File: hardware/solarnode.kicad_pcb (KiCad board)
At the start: 2 copper layers, 36 x 42.2 mm, 35 parts, among them IC1 STM32F0xxFxPx, P1 USB_OTG, P2 SWD, P3 C_PANEL, P4 C_BATT, U2 CN3083, U3 MCP1700, U4 RFM69HW, U5 DS18B20, U6 DS18B20

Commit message: Fix open-drain pull-ups to be actual pull-ups
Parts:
- P2: value SWD -> TC2030-CTX
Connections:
- R1 pad 1: GND -> VCC
- R2 pad 2: GND -> VCC
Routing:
- net VCC: track 76.8 -> 82.0 mm
- net GND: track 95.6 -> 92.0 mm, vias 13 -> 12
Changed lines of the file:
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@@
   (general
     (links 91)
-    (no_connects 0)
-    (area 159.245 94.875 205.390101 135.975)
+    (no_connects 1)
+    (area 161.674999 95.924999 197.825001 138.325001)
     (thickness 1.6)
     (drawings 9)
@@
     (mod_text_size 0.4 0.4)
     (mod_text_width 0.1)
-    (pad_size 3.3 3.3)
-    (pad_drill 3.3)
+    (pad_size 0.6 0.6)
+    (pad_drill 0.4)
     (pad_to_mask_clearance 0.2)
     (aux_axis_origin 161.75 138.25)
@@
       (effects (font (size 0.4 0.4) (thickness 0.1)))
     )
-    (fp_text value SWD (at 1.54 -2.516 90) (layer F.SilkS)
+    (fp_text value TC2030-CTX (at 1.54 -2.516 90) (layer F.SilkS)
       (effects (font (size 0.4 0.4) (thickness 0.1)))
     )
@@
     (fp_line (start -0.6 -0.875) (end 0.6 -0.875) (layer F.SilkS) (width 0.15))
     (pad 1 smd rect (at -0.95 0) (size 0.7 1.3) (layers F.Cu F.Paste F.Mask)
-      (net 2 GND))
+      (net 3 VCC))
     (pad 2 smd rect (at 0.95 0) (size 0.7 1.3) (layers F.Cu F.Paste F.Mask)
       (net 8 BATT_CHARGE))
@@
       (net 9 BATT_OK))
     (pad 2 smd rect (at 0.95 0 180) (size 0.7 1.3) (layers F.Cu F.Paste F.Mask)
-      (net 2 GND))
+      (net 3 VCC))
     (model Resistors_SMD.3dshapes/R_0805.wrl
       (at (xyz 0 0 0))
@@
   (segment (start 187 114) (end 183.815 114) (width 0.25) (layer F.Cu) (net 2))
   (segment (start 183.815 114) (end 183.7 114.115) (width 0.25) (layer F.Cu) (net 2))
-  (segment (start 173.55 115.25) (end 173.55 116.5) (width 0.25) (layer F.Cu) (net 2))
-  (segment (start 173.55 114) (end 173.55 115.25) (width 0.25) (layer F.Cu) (net 2))
-  (segment (start 173.55 115.25) (end 172.5 115.25) (width 0.25) (layer F.Cu) (net 2))
-  (via (at 172.5 115.25) (size 0.6) (drill 0.4) (layers F.Cu B.Cu) (net 2))
   (segment (start 181.75 109.5) (end 183 109.5) (width 0.5) (layer F.Cu) (net 2))
   (segment (start 183 109.5) (end 184.5 108) (width 0.5) (layer F.Cu) (net 2))
@@
   (segment (start 164.5 109.7) (end 164.5 111.2125) (width 0.25) (layer F.Cu) (net 2))
   (segment (start 164.5 111.2125) (end 164.25 111.4625) (width 0.25) (layer F.Cu) (net 2))
+  (segment (start 173 111.5) (end 173 113.45) (width 0.25) (layer F.Cu) (net 3))
+  (segment (start 173 113.45) (end 173.55 114) (width 0.25) (layer F.Cu) (net 3))
+  (segment (start 173.55 115.25) (end 173.55 116.5) (width 0.25) (layer F.Cu) (net 3))
+  (segment (start 173.55 114) (end 173.55 115.25) (width 0.25) (layer F.Cu) (net 3))
   (segment (start 180 123) (end 182 123) (width 0.25) (layer F.Cu) (net 3))
   (segment (start 180.552139 124.447861) (end 182 123) (width 0.25) (layer F.Cu) (net 3))

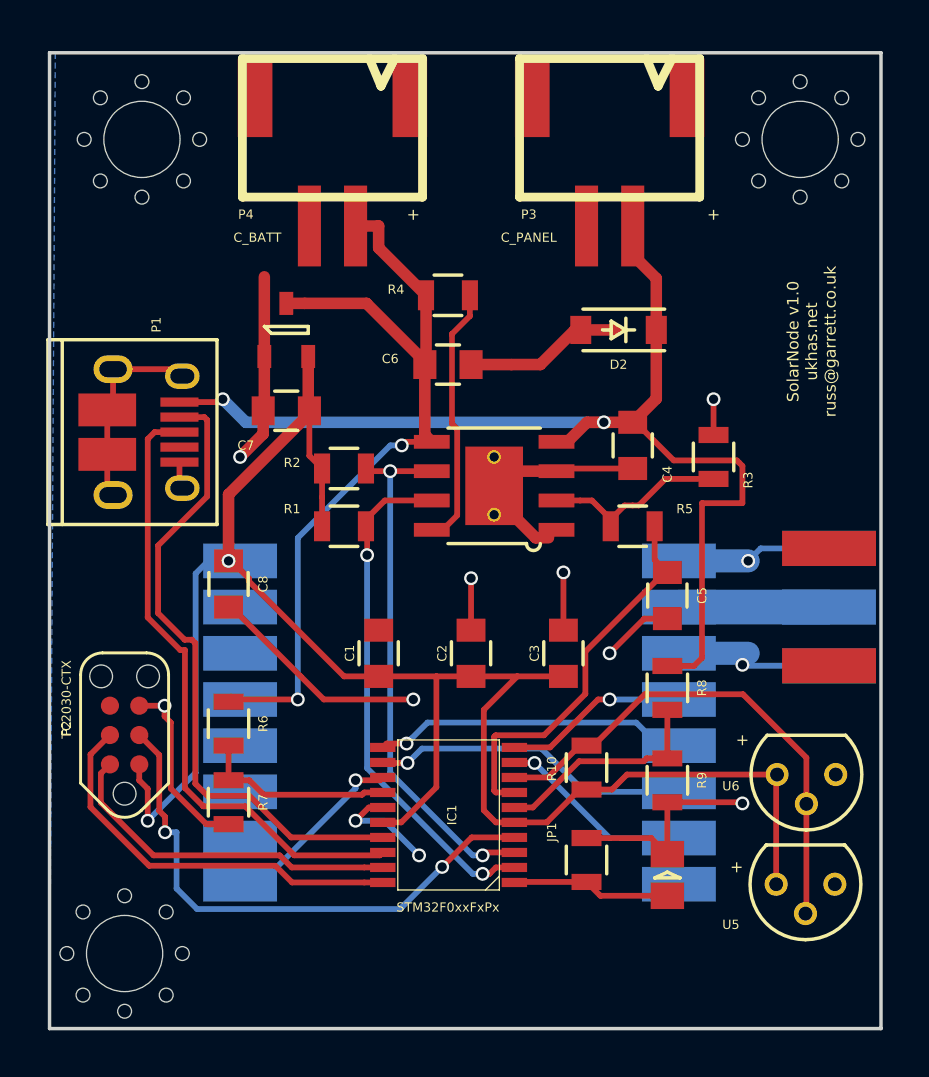
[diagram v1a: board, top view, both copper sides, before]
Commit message: Version 1.1
- Fix incorrect RFM69 SPI wiring
- Remove unneeded pullup resistors on CN3083 open-drain outputs
- Fix silk text sizing so it's actually readable
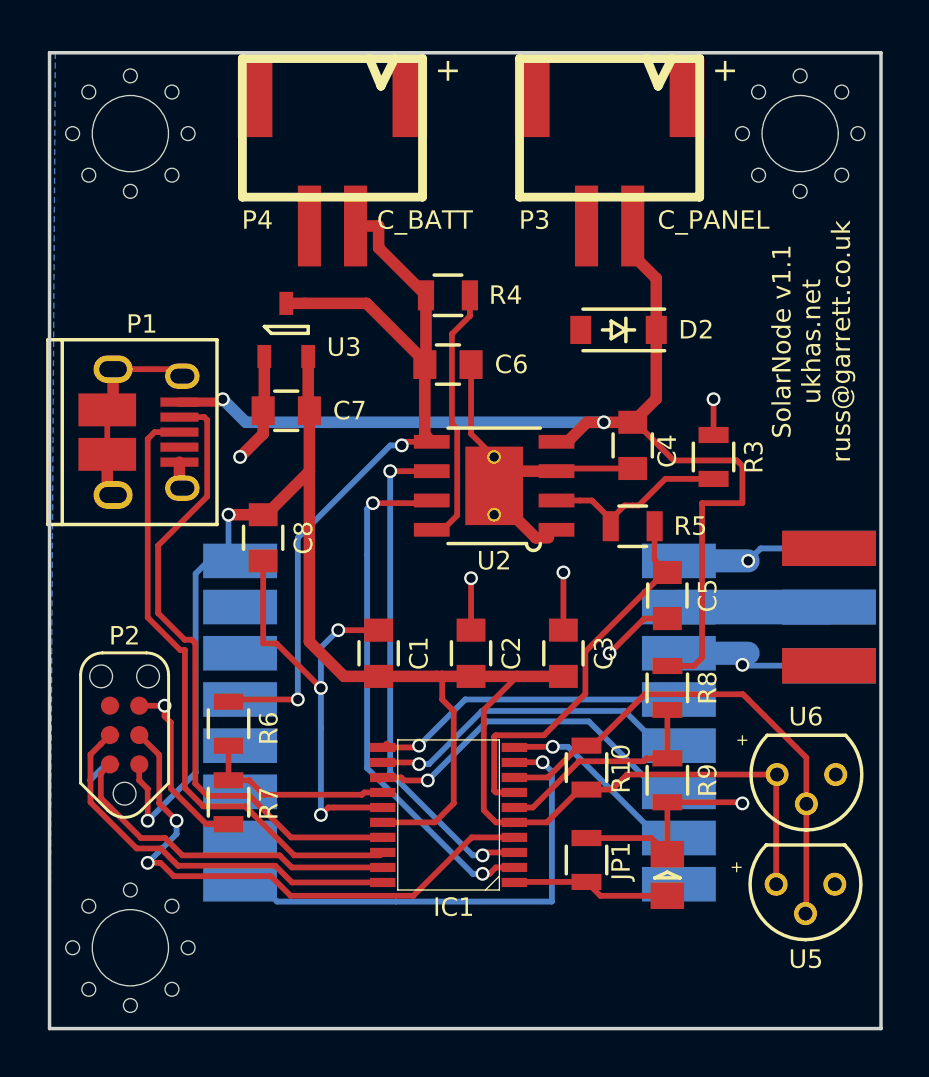
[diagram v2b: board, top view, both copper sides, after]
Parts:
- removed R1, R2: 10k, Resistors_SMD:R_0805
- removed the REF** at (194.2, 99.8)
- removed the REF** at (165.8, 99.8)
- removed the REF** at (165.0, 135.0)
- added REF**: M3_MOUNT, agg:M3_MOUNT, F.Cu at (194.2, 99.5)
- added REF**: M3_MOUNT, agg:M3_MOUNT, F.Cu at (165.2, 134.8)
- added REF**: M3_MOUNT, agg:M3_MOUNT, F.Cu at (165.2, 99.5)
- moved C8 2.50 mm to (171.0, 117.0)
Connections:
- IC1 pad 9: Net-(IC1-Pad9) -> RFM_RST
- P1 pad 4: Net-(P1-Pad4) -> (no net)
- P2 pad 6: Net-(P2-Pad6) -> (no net)
- U4 pad 1: Net-(U4-Pad1) -> (no net)
- U4 pad 10: Net-(U4-Pad10) -> (no net)
- U4 pad 11: Net-(U4-Pad11) -> (no net)
- U4 pad 12: Net-(U4-Pad12) -> (no net)
- U4 pad 13: Net-(U4-Pad13) -> (no net)
- U4 pad 14: Net-(U4-Pad14) -> (no net)
- U4 pad 15: Net-(U4-Pad15) -> (no net)
- U4 pad 2: Net-(IC1-Pad9) -> Net-(IC1-Pad10)
- U4 pad 3: Net-(IC1-Pad12) -> Net-(IC1-Pad13)
- U4 pad 4: Net-(IC1-Pad11) -> Net-(IC1-Pad12)
- U4 pad 5: Net-(IC1-Pad10) -> Net-(IC1-Pad11)
- U4 pad 9: Net-(IC1-Pad13) -> RFM_RST
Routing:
- net RFM_RST: track 0.00 -> 21.3 mm, vias 0 -> 1
- net Net-(IC1-Pad9): track 11.0 -> 0.00 mm, vias 1 -> 0
- net Net-(IC1-Pad13): track 8.30 -> 15.4 mm
- net BATT_OK: track 22.9 -> 21.8 mm
- net (no net): track 0.00 -> 1.06 mm
- net GND: track 92.0 -> 91.2 mm
- net Net-(IC1-Pad10): track 7.98 -> 8.77 mm
- net Net-(IC1-Pad12): track 13.9 -> 14.5 mm
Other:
- board text added: "SolarNode v1.1 ukhas.net russ@garrett.co.uk"
- board text removed: "SolarNode v1.0 ukhas.net russ@garrett.co.uk"

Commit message: Version 1.1 hardware + stencil
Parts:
- removed JP1: Boot, Resistors_SMD:R_0805
- IC1: value STM32F0xxFxPx -> STM32F042F6P6
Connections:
- P1 pad 4: (no net) -> Net-(P1-Pad4)
- P2 pad 6: (no net) -> Net-(P2-Pad6)
- U4 pad 1: (no net) -> Net-(U4-Pad1)
- U4 pad 10: (no net) -> Net-(U4-Pad10)
- U4 pad 11: (no net) -> Net-(U4-Pad11)
- U4 pad 12: (no net) -> Net-(U4-Pad12)
- U4 pad 13: (no net) -> Net-(U4-Pad13)
- U4 pad 14: (no net) -> Net-(U4-Pad14)
- U4 pad 15: (no net) -> Net-(U4-Pad15)
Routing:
- net GND: track 91.2 -> 87.4 mm
- net +BATT: track 36.1 -> 34.6 mm
